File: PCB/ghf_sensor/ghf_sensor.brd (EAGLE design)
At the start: 72.1 x 48.2 mm, 14 parts, among them IC1 MAX481CPA, J1 MH-Z19-CO2-NDIR-SENSOR, T1 BPX81, X1 SoilSens, X2 RS485

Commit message: PCB modified
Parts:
- removed R5: (no value), resistor:0204/7
- added R6: 10k, rcl:0204/5
- added R7: 4.7k, rcl:0204/5
- added R8: 100, rcl:0204/5
- added T2: (no value), transistor:TO92
- turned U$1 to 0 degrees
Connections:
- removed net N$12: R5.1, X2.1
- new net N$13: IC1.2, IC1.3, R6.2, T2.3
- new net N$14: R7.2, T2.2
- new net N$15: IC1.4, R7.1, U$2.TX0
- new net N$16: R8.2, U$2.A1
- net +5V: now also R6.1, U$1.1, X2.1; no longer R5.2
- net GND: now also T2.1
- net N$8: now also R8.1, X1.3; no longer IC1.4, U$2.TX0
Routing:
- net +5V: track 138.2 -> 177.1 mm, vias 0 -> 1
- net N$16: track 0.00 -> 38.2 mm
- net N$11: track 61.8 -> 30.5 mm, vias 0 -> 2
- net N$15: track 0.00 -> 26.5 mm
- net N$13: track 0.00 -> 22.1 mm
- net N$1: track 38.2 -> 52.4 mm
- net GND: track 0.00 -> 14.1 mm
- net N$12: track 4.46 -> 0.00 mm, vias 0 -> 1
- net N$14: track 0.00 -> 3.17 mm
- net N$8: track 7.40 -> 9.96 mm
- net N$10: track 29.5 -> 32.0 mm

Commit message: PCB
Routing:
- net GND: track 14.1 -> 234.9 mm
- net N$17: track 0.00 -> 0.83 mm
- net N$15: track 26.5 -> 26.1 mm, vias 0 -> 2
- added copper zone on layer 16, net N$17
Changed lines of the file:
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@@
 <contactref element="R2" pad="2"/>
 <contactref element="IC1" pad="5"/>
-<polygon width="0.4064" layer="16">
-<vertex x="0" y="48.26"/>
-<vertex x="71.12" y="48.26"/>
-<vertex x="71.12" y="0"/>
-<vertex x="0" y="0"/>
-<vertex x="0" y="1.27"/>
-</polygon>
 <contactref element="T2" pad="1"/>
 <wire x1="52.07" y1="17.78" x2="54.61" y2="16.39" width="0.4064" layer="16"/>
-<wire x1="54.61" y1="16.39" x2="59.57" y2="6.35" width="0.4064" layer="16"/>
+<wire x1="54.61" y1="16.39" x2="57.07794375" y2="11.394403125" width="0.4064" layer="16"/>
+<wire x1="57.07794375" y1="11.394403125" x2="59.57" y2="6.35" width="0.4064" layer="16"/>
+<wire x1="40.64" y1="15.24" x2="40.64" y2="20.32" width="0.254" layer="16"/>
+<wire x1="38.1" y1="15.24" x2="40.64" y2="15.24" width="0.254" layer="16"/>
+<wire x1="38.1" y1="11.43" x2="38.1" y2="15.24" width="0.254" layer="16"/>
+<wire x1="57.15" y1="11.43" x2="38.1" y2="11.43" width="0.254" layer="16"/>
+<wire x1="57.15" y1="11.43" x2="57.07794375" y2="11.394403125" width="0.254" layer="16"/>
+<wire x1="12.7" y1="46.99" x2="12.7" y2="44.45" width="0.254" layer="16"/>
+<wire x1="20.32" y1="46.99" x2="12.7" y2="46.99" width="0.254" layer="16"/>
+<wire x1="21.59" y1="45.72" x2="20.32" y2="46.99" width="0.254" layer="16"/>
+<wire x1="21.59" y1="43.18" x2="21.59" y2="45.72" width="0.254" layer="16"/>
+<wire x1="22.86" y1="41.91" x2="21.59" y2="43.18" width="0.254" layer="16"/>
+<wire x1="27.94" y1="41.91" x2="22.86" y2="41.91" width="0.254" layer="16"/>
+<wire x1="29.21" y1="43.18" x2="27.94" y2="41.91" width="0.254" layer="16"/>
+<wire x1="30.48" y1="41.91" x2="29.21" y2="43.18" width="0.254" layer="16"/>
+<wire x1="31.75" y1="43.18" x2="30.48" y2="41.91" width="0.254" layer="16"/>
+<wire x1="33.02" y1="41.91" x2="31.75" y2="43.18" width="0.254" layer="16"/>
+<wire x1="34.29" y1="41.91" x2="33.02" y2="41.91" width="0.254" layer="16"/>
+<wire x1="35.56" y1="40.64" x2="34.29" y2="41.91" width="0.254" layer="16"/>
+<wire x1="35.56" y1="39.37" x2="35.56" y2="40.64" width="0.254" layer="16"/>
+<wire x1="66.04" y1="39.37" x2="50.8" y2="39.37" width="0.254" layer="16"/>
+<wire x1="50.8" y1="39.37" x2="35.56" y2="39.37" width="0.254" layer="16"/>
+<wire x1="46.99" y1="33.02" x2="46.99" y2="35.56" width="0.254" layer="16"/>
+<wire x1="49.53" y1="33.02" x2="46.99" y2="33.02" width="0.254" layer="16"/>
+<wire x1="50.8" y1="34.29" x2="49.53" y2="33.02" width="0.254" layer="16"/>
+<wire x1="50.8" y1="39.37" x2="50.8" y2="34.29" width="0.254" layer="16"/>
+<wire x1="68.58" y1="6.35" x2="59.57" y2="6.35" width="0.254" layer="16"/>
+<wire x1="69.85" y1="7.62" x2="68.58" y2="6.35" width="0.254" layer="16"/>
+<wire x1="69.85" y1="39.37" x2="69.85" y2="7.62" width="0.254" layer="16"/>
+<wire x1="66.04" y1="39.37" x2="69.85" y2="39.37" width="0.254" layer="16"/>
+<wire x1="66.04" y1="39.37" x2="66.04" y2="39.25" width="0.254" layer="16"/>
+<wire x1="5.08" y1="12.7" x2="5.08" y2="17.78" width="0.254" layer="16"/>
+<wire x1="6.35" y1="8.89" x2="7.62" y2="8.89" width="0.254" layer="16"/>
+<wire x1="5.08" y1="10.16" x2="6.35" y2="8.89" width="0.254" layer="16"/>
+<wire x1="5.08" y1="12.7" x2="5.08" y2="10.16" width="0.254" layer="16"/>
+<wire x1="7.62" y1="8.89" x2="7.62" y2="8.6" width="0.254" layer="16"/>
+<wire x1="5.08" y1="12.7" x2="5.37" y2="12.7" width="0.254" layer="16"/>
+<wire x1="12.7" y1="44.45" x2="12.7" y2="34.29" width="0.4064" layer="16"/>
+<wire x1="12.7" y1="34.29" x2="3.81" y2="34.29" width="0.4064" layer="16"/>
+<wire x1="3.81" y1="34.29" x2="3.81" y2="40.64" width="0.4064" layer="16"/>
+<wire x1="3.81" y1="40.64" x2="0" y2="40.64" width="0.4064" layer="16"/>
+<wire x1="0" y1="40.64" x2="0" y2="17.78" width="0.4064" layer="16"/>
+<wire x1="0" y1="17.78" x2="5.08" y2="17.78" width="0.4064" layer="16"/>
+<polygon width="0.4064" layer="16" isolate="0.8128">
+<vertex x="0" y="48.26"/>
+<vertex x="72.39" y="48.26"/>
+<vertex x="72.39" y="0"/>
+<vertex x="0" y="0"/>
+</polygon>
 </signal>
 <signal name="N$1">
@@
 <wire x1="5.08" y1="27.94" x2="8.89" y2="27.94" width="0.254" layer="16"/>
 <wire x1="5.08" y1="25.4" x2="5.08" y2="27.94" width="0.254" layer="16"/>
-<wire x1="2.54" y1="40.64" x2="2.54" y2="44.45" width="0.254" layer="16"/>
-<wire x1="3.81" y1="40.64" x2="2.54" y2="40.64" width="0.254" layer="16"/>
-<wire x1="5.08" y1="39.37" x2="3.81" y2="40.64" width="0.254" layer="16"/>
-<wire x1="5.08" y1="27.94" x2="5.08" y2="39.37" width="0.254" layer="16"/>
+<wire x1="3.81" y1="44.45" x2="2.54" y2="44.45" width="0.254" layer="16"/>
+<wire x1="5.08" y1="39.37" x2="3.81" y2="44.45" width="0.254" layer="16"/>
+<wire x1="5.08" y1="27.94" x2="5.08" y2="39.37" width="0.254" layer="1"/>
+<via x="5.08" y="39.37" extent="1-16" drill="0.6" shape="square"/>
+<via x="5.08" y="27.94" extent="1-16" drill="0.6" shape="square"/>
 </signal>
 <signal name="N$8">
@@
 <via x="39.37" y="7.62" extent="1-16" drill="0.6" shape="square"/>
 </signal>
+<signal name="N$17">
+<polygon width="0.4064" layer="16" isolate="0.8128">
+<vertex x="0" y="48.26"/>
+<vertex x="72.39" y="48.26"/>
+<vertex x="72.39" y="0"/>
+<vertex x="0" y="0"/>
+</polygon>
+<wire x1="11.43" y1="11.43" x2="11.635996875" y2="10.87755625" width="0.254" layer="16"/>
+<wire x1="12.7" y1="10.16" x2="12.526775" y2="9.986775" width="0.254" layer="16"/>
+</signal>
 </signals>

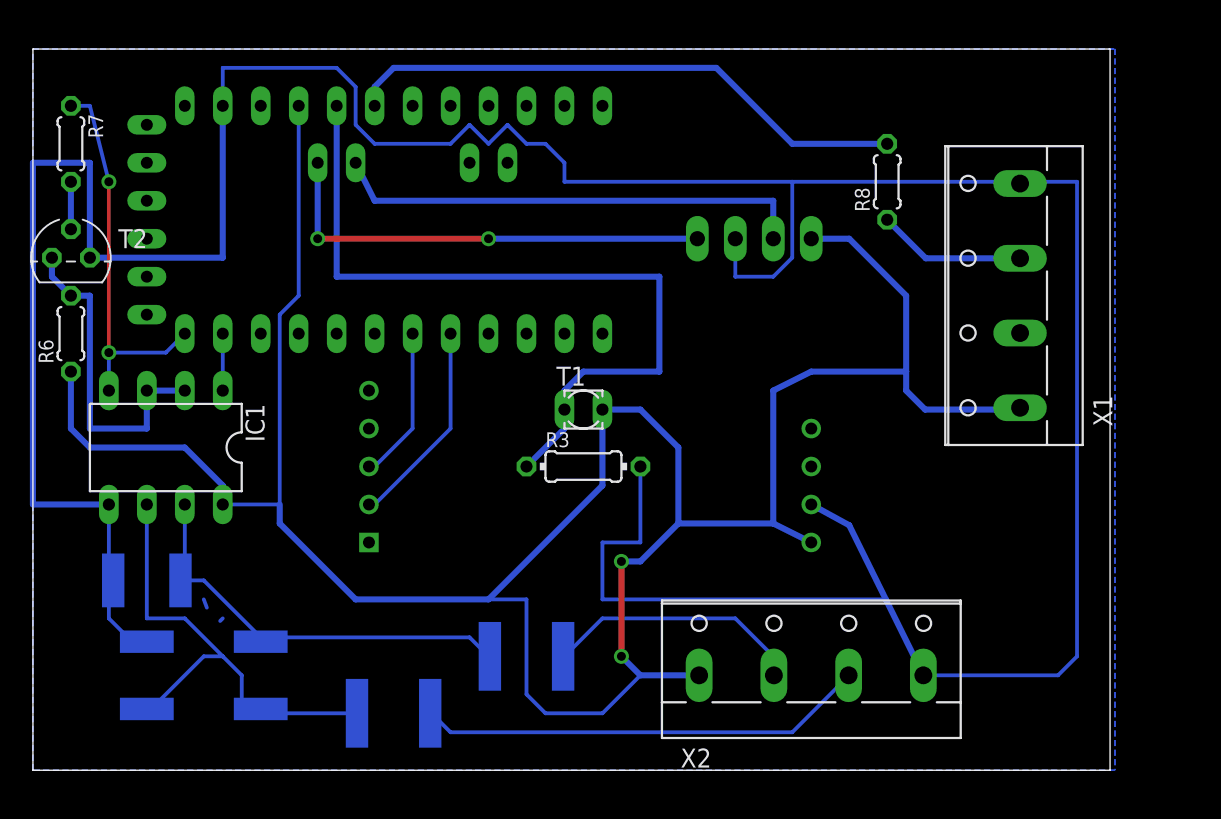
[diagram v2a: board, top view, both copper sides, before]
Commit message: add cad data, modify PCB board and schematic
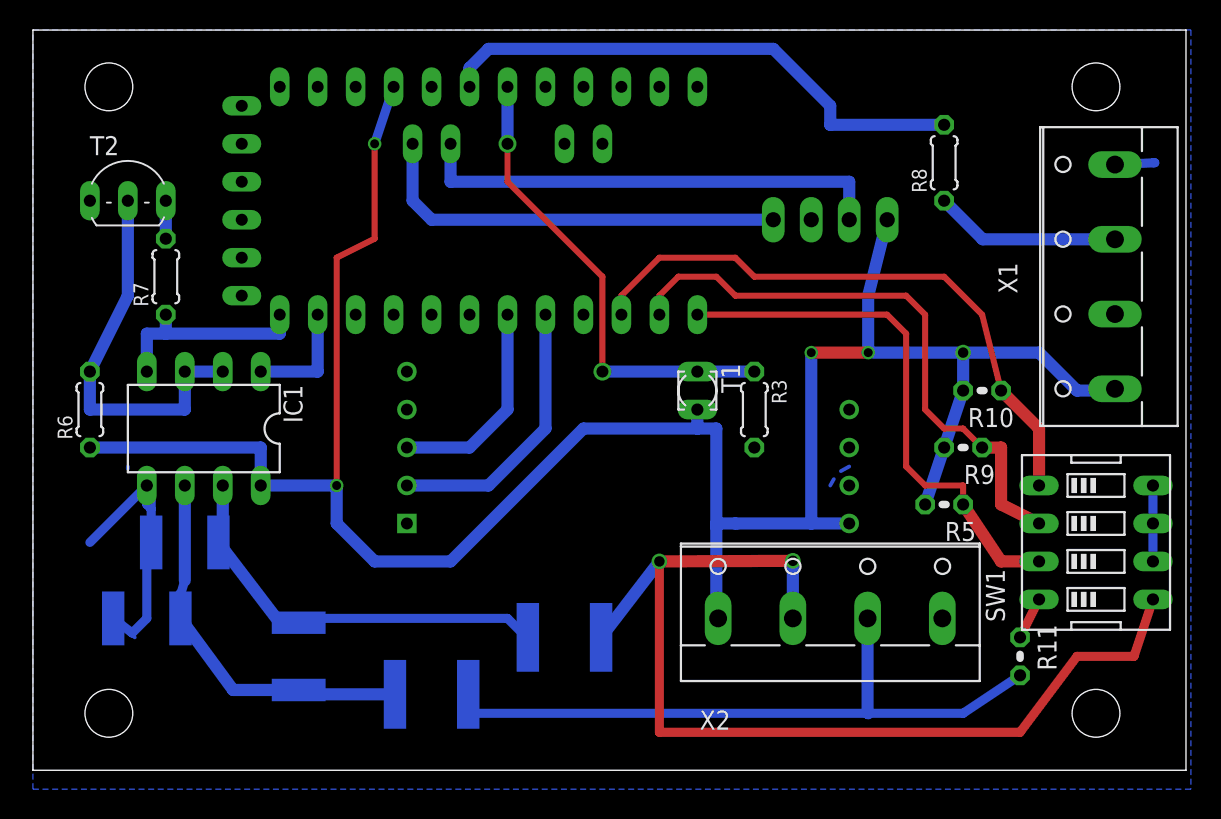
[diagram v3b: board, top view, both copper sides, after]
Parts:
- added R10, R5, R9: 100k, rcl:0204V
- added R11: 120, rcl:0204V
- added SW1: (no value), special:EDG-04
- R1, R2, R4: value VARISTORCN1812 -> TVS
- R3: device rcl:0204/7 -> rcl:0204/5
- T2: device transistor:TO92 -> transistor:TO92-ECB
- moved R3 12.0 mm to (48.3, 24.1), turned to 270 degrees
- moved R7 10.9 mm to (8.89, 33.0), turned to 90 degrees
- moved T1 7.73 mm to (44.5, 25.4), turned to 270 degrees
- moved X1 6.48 mm to (71.1, 33.0)
- moved U$2 6.48 mm to (29.2, 39.4)
- moved T2 5.39 mm to (6.35, 38.1)
- moved U$1 5.24 mm to (53.3, 36.8)
- moved R6 5.24 mm to (3.81, 24.1)
- moved R8 4.02 mm to (61.0, 40.6)
- moved X2 4.02 mm to (53.3, 11.4)
- moved R2 3.81 mm to (7.62, 10.2), turned to 0 degrees
- moved R1 3.59 mm to (10.2, 15.2)
- moved U$3 2.84 mm to (26.7, 5.08)
- moved R4 2.84 mm to (17.8, 7.62)
- moved J1 2.84 mm to (54.6, 16.5)
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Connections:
- removed net N$4: U$4.1, X2.2
- removed net N$5: U$3.1, X2.3
- new net N$12: R5.1, SW1.3, U$2.D9
- new net N$18: R9.1, SW1.2, U$2.D8
- new net N$19: R10.1, SW1.1, U$2.D7
- new net N$2: SW1.5, U$4.1, X2.2
- new net N$20: R11.1, SW1.4
- new net N$3: R11.2, U$3.1, X2.3
- net +5V: now also R10.2, R5.2, R9.2
- net GND: now also SW1.6, SW1.7, SW1.8, T2.E; no longer T2.1
- net N$1: now also U$2.A2; no longer U$2.A0
- net N$13: now also T2.C; no longer T2.3
- net N$14: now also T2.B; no longer T2.2
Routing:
- net GND: track 234.9 -> 30.2 mm
- net N$2: track 0.00 -> 68.9 mm, vias 0 -> 2
- net N$3: track 0.00 -> 45.3 mm
- net N$19: track 0.00 -> 40.7 mm
- net N$18: track 0.00 -> 39.8 mm
- net N$12: track 0.00 -> 36.1 mm, vias 1 -> 0
- net N$5: track 30.2 -> 0.00 mm
- net +5V: track 177.1 -> 155.8 mm, vias 1 -> 5
- net N$1: track 52.4 -> 31.8 mm, vias 0 -> 2
- net N$4: track 17.5 -> 0.00 mm
- net N$15: track 26.1 -> 14.0 mm, vias 2 -> 0
- net N$22: track 33.0 -> 26.0 mm
- net N$7: track 13.9 -> 18.5 mm
- net N$13: track 22.1 -> 26.0 mm
- net N$6: track 10.3 -> 14.1 mm
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- removed copper zone on layer 16, net N$17
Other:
- board size 72.1 x 48.2 mm -> 77.1 x 49.5 mm
